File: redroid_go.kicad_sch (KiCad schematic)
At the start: 100 parts, among them J1 USB4105-GF-A, J2 5051101892, J3 Conn_01x02_Pin, J4 Conn_01x10_Pin, Q1 UMH3N, Q2 PMOS, Q3 UMH3N, SW1 UP, SW10 A, SW11 SW_SPDT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

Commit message: Rename label
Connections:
- net IO21 renamed D/C
- net D/C: no longer U1.33 (IO21)
- new net D/C: U1.33 (IO21)
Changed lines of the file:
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@@
 		)
 	)
-	(global_label "IO21"
+	(global_label "D/C"
 		(shape input)
 		(at 240.03 154.94 180)
@@
 		)
 	)
-	(global_label "IO21"
+	(global_label "D{slash}C"
 		(shape input)
 		(at 129.54 76.2 0)
@@
 		)
 		(property "Intersheetrefs" "${INTERSHEET_REFS}"
-			(at 136.8795 76.2 0)
-			(effects
-				(font
+			(at 136.3957 76.2 0)
+			(effects
+				(font

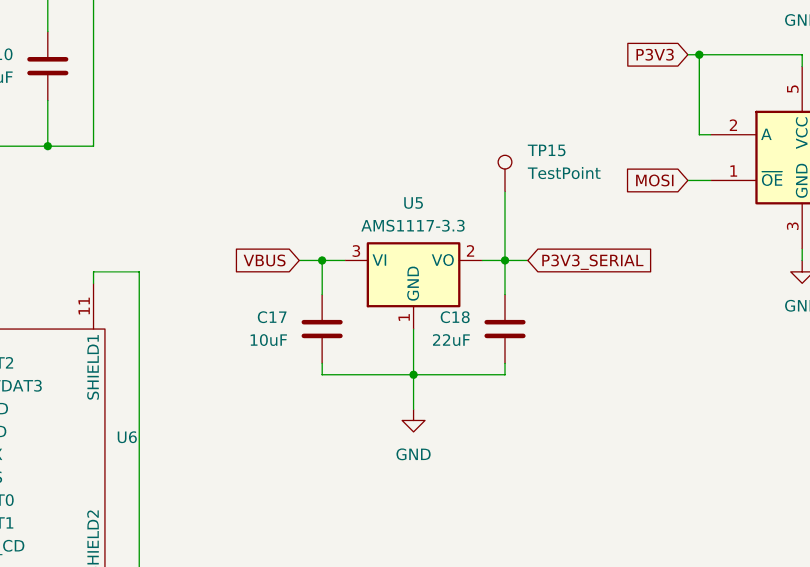
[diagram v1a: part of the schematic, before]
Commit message: Change serial LDO to SOT23-3 and update BOM
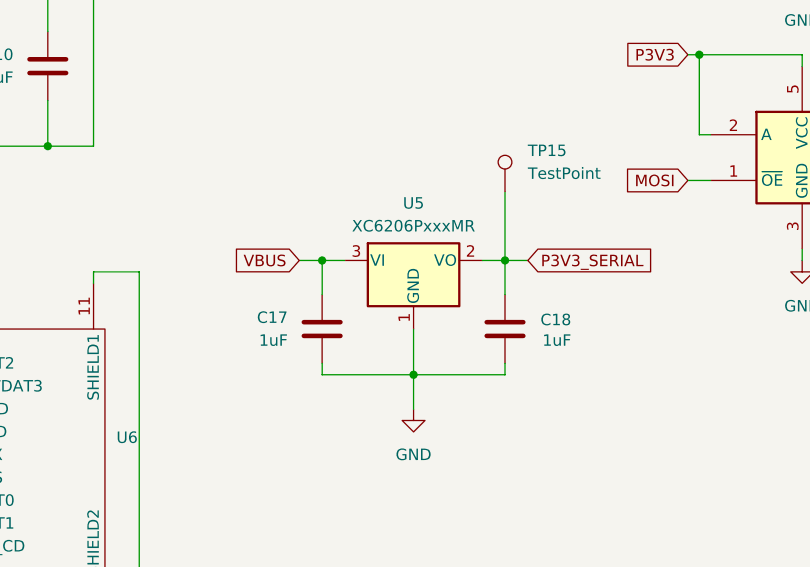
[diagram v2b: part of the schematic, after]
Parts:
- removed U5: AMS1117-3.3, Package_TO_SOT_SMD:SOT-223-3_TabPin2, symbol Regulator_Linear:AMS1117-3.3
- added U5: XC6206PxxxMR, Package_TO_SOT_SMD:SOT-23-3, symbol Regulator_Linear:XC6206PxxxMR
- C17: value 10uF -> 1uF
- C18: value 22uF -> 1uF
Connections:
- net GND: now also U5.1 (GND)
- net P3V3_SERIAL: now also U5.2 (VO)
- net VBUS: now also U5.3 (VI)
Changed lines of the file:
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@@
 			)
 		)
-		(property "Value" "10uF"
+		(property "Value" "1uF"
 			(at 267.97 236.2199 0)
 			(effects
@@
 		(dnp no)
 		(property "Reference" "C18"
-			(at 288.29 233.6799 0)
+			(at 299.466 233.934 0)
 			(effects
 				(font
@@
 			)
 		)
-		(property "Value" "22uF"
-			(at 288.29 236.2199 0)
+		(property "Value" "1uF"
+			(at 299.466 236.22 0)
 			(effects
 				(font
@@
 	)
 	(symbol
-		(lib_id "Regulator_Linear:AMS1117-3.3")
-		(at 281.94 227.33 0)
-		(unit 1)
-		(exclude_from_sim no)
-		(in_bom yes)
-		(on_board yes)
-		(dnp no)
-		(fields_autoplaced yes)
-		(property "Reference" "U5"
-			(at 281.94 220.98 0)
-			(effects
-				(font
-					(size 1.27 1.27)
-				)
-			)
-		)
-		(property "Value" "AMS1117-3.3"
-			(at 281.94 223.52 0)
-			(effects
-				(font
-					(size 1.27 1.27)
-				)
-			)
-		)
-		(property "Footprint" "Package_TO_SOT_SMD:SOT-223-3_TabPin2"
-			(at 281.94 222.25 0)
-			(effects
-				(font
-					(size 1.27 1.27)
-				)
-				(hide yes)
-			)
-		)
-		(property "Datasheet" "http://www.advanced-monolithic.com/pdf/ds1117.pdf"
-			(at 284.48 233.68 0)
-			(effects
-				(font
-					(size 1.27 1.27)
-				)
-				(hide yes)
-			)
-		)
-		(property "Description" "1A Low Dropout regulator, positive, 3.3V fixed output, SOT-223"
-			(at 281.94 227.33 0)
-			(effects
-				(font
-					(size 1.27 1.27)
-				)
-				(hide yes)
-			)
-		)
-		(pin "3"
-		)
-		(pin "2"
-		)
-		(pin "1"
-		)
-		(instances
-			(project ""
-				(path "/54323edd-924e-4c99-bcbf-5375689f8e73"
-					(reference "U5")
-					(unit 1)
-				)
-			)
-		)
-	)
-	(symbol
 		(lib_id "Device:C")
 		(at 22.86 46.99 0)
@@
 					(unit 1)
 				)
+			)
+		)
+	)
+	(symbol
+		(lib_id "Regulator_Linear:XC6206PxxxMR")
+		(at 281.94 227.33 0)
+		(unit 1)
+		(exclude_from_sim no)
+		(in_bom yes)
+		(on_board yes)
+		(dnp no)
+		(fields_autoplaced yes)
+		(property "Reference" "U5"
+			(at 281.94 220.98 0)
+			(effects
+				(font
+					(size 1.27 1.27)
+				)
+			)
+		)
+		(property "Value" "XC6206PxxxMR"
+			(at 281.94 223.52 0)
+			(effects
+				(font
+					(size 1.27 1.27)
+				)
+			)
+		)
+		(property "Footprint" "Package_TO_SOT_SMD:SOT-23-3"
+			(at 281.94 221.615 0)
+			(effects
+				(font
+					(size 1.27 1.27)
+					(italic yes)
+				)
+				(hide yes)
+			)
+		)
+		(property "Datasheet" "https://www.torexsemi.com/file/xc6206/XC6206.pdf"
+			(at 281.94 227.33 0)
+			(effects
+				(font
+					(size 1.27 1.27)
+				)
+				(hide yes)
+			)
+		)
+		(property "Description" "Positive 60-250mA Low Dropout Regulator, Fixed Output, SOT-23"
+			(at 281.94 227.33 0)
+			(effects
+				(font
+					(size 1.27 1.27)
+				)
+				(hide yes)
+			)
+		)
+		(pin "2"
+		)
+		(pin "1"
+		)
+		(pin "3"
+		)
+		(instances
+			(project ""
+				(path "/54323edd-924e-4c99-bcbf-5375689f8e73"
+					(reference "U5")
+					(unit 1)
+				)
